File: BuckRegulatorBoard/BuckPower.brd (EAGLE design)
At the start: 41.6 x 31.7 mm, 5 parts, among them U1 LM2574N

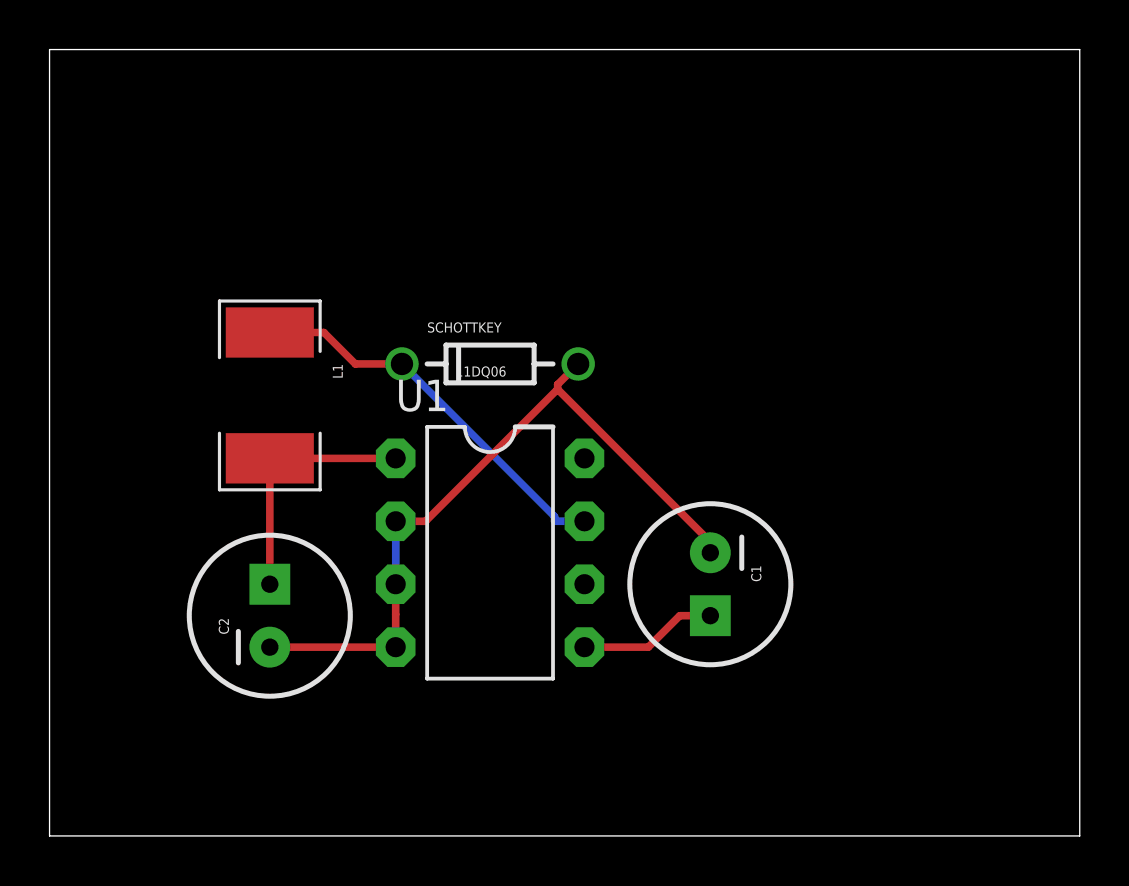
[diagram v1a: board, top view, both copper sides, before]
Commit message: Tested versions of breakout boards
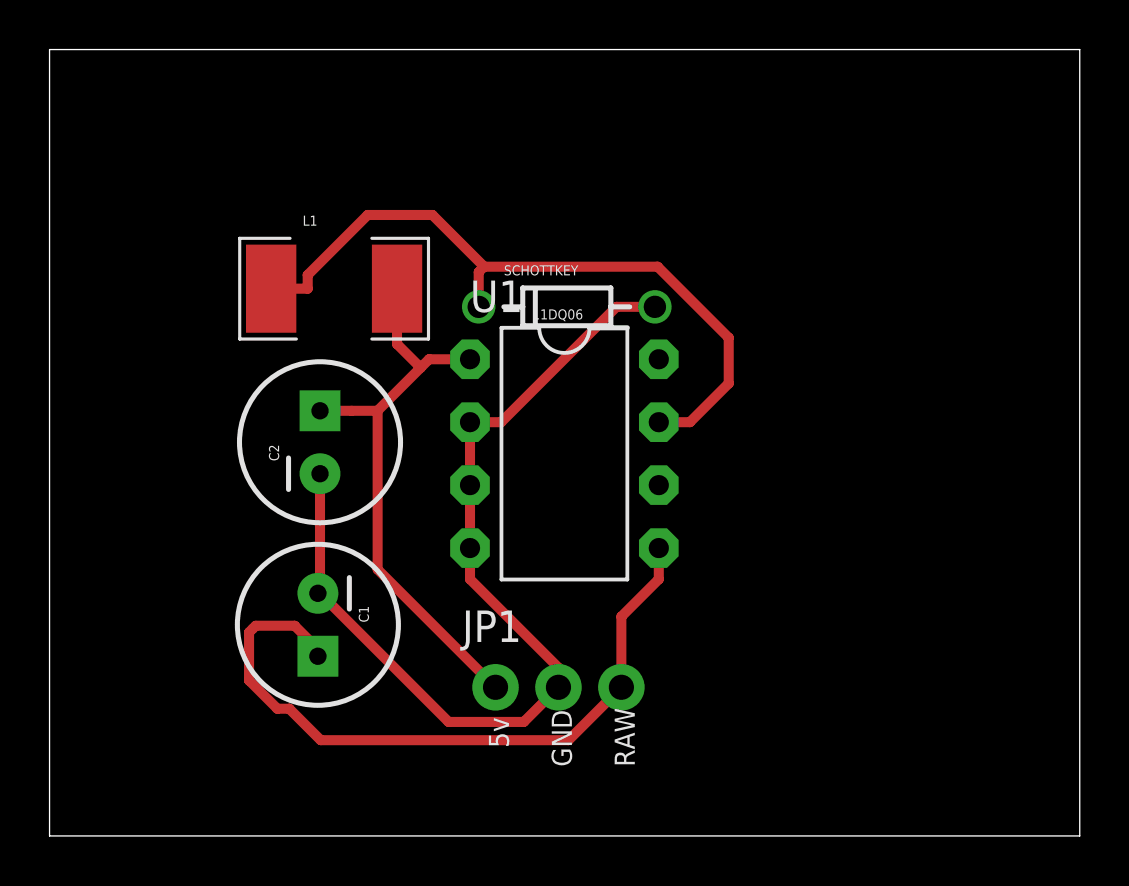
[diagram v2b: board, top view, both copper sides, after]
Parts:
- added JP1: (no value), SparkFun:1X03_NO_SILK
- moved C1 15.9 mm to (10.8, 8.52)
- moved C2 7.29 mm to (10.9, 15.9)
- moved L1 5.03 mm to (11.5, 22.1), turned to 0 degrees
- moved U1 5.00 mm to (20.8, 15.4)
- moved SCHOTTKEY 3.86 mm to (20.9, 21.4)
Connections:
- net GND: now also JP1.2
- net RAW: now also JP1.3
- net VCC: now also JP1.1
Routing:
- net RAW: track 5.61 -> 28.7 mm
- net VCC: track 10.2 -> 23.6 mm
- net N$1: track 16.0 -> 29.1 mm
- net GND: track 29.4 -> 38.8 mm
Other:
- board text added: "5v"
- board text added: "GND"
- board text added: "RAW"
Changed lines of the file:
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@@
 <setting verticaltext="up"/>
 </settings>
-<grid distance="1" unitdist="mm" unit="mm" style="lines" multiple="1" display="yes" altdistance="0.025" altunitdist="inch" altunit="inch"/>
+<grid distance="10" unitdist="mil" unit="mil" style="lines" multiple="1" display="yes" altdistance="1" altunitdist="mil" altunit="mil"/>
 <layers>
 <layer number="1" name="Top" color="4" fill="1" visible="yes" active="yes"/>
@@
 <wire x1="41.58" y1="31.74" x2="0" y2="31.74" width="0" layer="20"/>
 <wire x1="0" y1="31.74" x2="0" y2="0" width="0" layer="20"/>
+<rectangle x1="13.1064" y1="24.3078" x2="15.2654" y2="24.5618" layer="41"/>
+<rectangle x1="25.7048" y1="18.5166" x2="26.8986" y2="19.8628" layer="41"/>
+<text x="18.542" y="3.556" size="0.8128" layer="25" ratio="10" rot="R90">5v</text>
+<text x="21.082" y="2.794" size="0.8128" layer="25" ratio="10" rot="R90">GND</text>
+<text x="23.622" y="2.794" size="0.8128" layer="25" ratio="10" rot="R90">RAW</text>
 </plain>
 <attributes>
@@
 </autorouter>
 <elements>
-<element name="U1" library="Dustin" package="8DILL" value="LM2574N" x="17.78" y="11.43" rot="R270"/>
-<element name="C1" library="SparkFun" package="CPOL-RADIAL-100UF-25V" value="22uf" x="26.67" y="10.16" rot="R270"/>
-<element name="C2" library="SparkFun" package="CPOL-RADIAL-100UF-25V" value="220uf" x="8.89" y="8.89" rot="R90"/>
-<element name="L1" library="SparkFun" package="INDUCTOR-1206" value="330uH" x="8.89" y="17.78" rot="R270"/>
-<element name="SCHOTTKEY" library="SparkFun" package="DIODE-ZENER" value="11DQ06" x="17.78" y="19.05"/>
+<element name="U1" library="Dustin" package="8DILL" value="LM2574N" x="20.78" y="15.43" rot="R270"/>
+<element name="C1" library="SparkFun" package="CPOL-RADIAL-100UF-25V" value="22uf" x="10.8311" y="8.5228" rot="R270"/>
+<element name="C2" library="SparkFun" package="CPOL-RADIAL-100UF-25V" value="220uf" x="10.9165" y="15.89" rot="R90"/>
+<element name="L1" library="SparkFun" package="INDUCTOR-1206" value="330uH" x="11.485" y="22.089"/>
+<element name="SCHOTTKEY" library="SparkFun" package="DIODE-ZENER" value="11DQ06" x="20.8769" y="21.3553"/>
+<element name="JP1" library="SparkFun" package="1X03_NO_SILK" value="" x="18" y="6"/>
 </elements>
 <signals>
@@
 <contactref element="U1" pad="5"/>
 <contactref element="C1" pad="1"/>
-<wire x1="26.67" y1="8.89" x2="25.438" y2="8.89" width="0.3048" layer="1"/>
-<wire x1="21.59" y1="7.62" x2="24.168" y2="7.62" width="0.3048" layer="1"/>
-<wire x1="24.168" y1="7.62" x2="25.438" y2="8.89" width="0.3048" layer="1"/>
+<contactref element="JP1" pad="3"/>
+<wire x1="8.2024" y1="8.3661" x2="8.0517" y2="8.2154" width="0.4064" layer="1"/>
+<wire x1="8.0517" y1="8.2154" x2="8.0517" y2="6.277" width="0.4064" layer="1"/>
+<wire x1="8.0517" y1="6.277" x2="9.1946" y2="5.1341" width="0.4064" layer="1"/>
+<wire x1="9.1946" y1="5.1341" x2="9.6773" y2="5.1341" width="0.4064" layer="1"/>
+<wire x1="9.6773" y1="5.1341" x2="9.6773" y2="5.134" width="0.4064" layer="1"/>
+<wire x1="9.6773" y1="5.134" x2="10.9461" y2="3.8652" width="0.4064" layer="1"/>
+<wire x1="10.9461" y1="3.8652" x2="20.9452" y2="3.8652" width="0.4064" layer="1"/>
+<wire x1="20.9452" y1="3.8652" x2="23.08" y2="6" width="0.4064" layer="1"/>
+<wire x1="10.8311" y1="7.2528" x2="10.8311" y2="7.5486" width="0.4064" layer="1"/>
+<wire x1="10.8311" y1="7.5486" x2="9.896" y2="8.4837" width="0.4064" layer="1"/>
+<wire x1="9.896" y1="8.4837" x2="8.32" y2="8.4837" width="0.4064" layer="1"/>
+<wire x1="8.32" y1="8.4837" x2="8.2024" y2="8.3661" width="0.4064" layer="1"/>
+<wire x1="24.59" y1="10.3626" x2="23.08" y2="8.8526" width="0.4064" layer="1"/>
+<wire x1="23.08" y1="8.8526" x2="23.08" y2="6" width="0.4064" layer="1"/>
+<wire x1="24.59" y1="11.62" x2="24.59" y2="10.3626" width="0.4064" layer="1"/>
 </signal>
 <signal name="GND">
@@
 <contactref element="U1" pad="3"/>
 <contactref element="SCHOTTKEY" pad="P$2"/>
-<wire x1="20.5065" y1="18.0299" x2="26.67" y2="11.8663" width="0.3048" layer="1"/>
-<wire x1="26.67" y1="11.8663" x2="26.67" y2="11.43" width="0.3048" layer="1"/>
-<wire x1="21.336" y1="19.05" x2="20.5064" y2="18.2204" width="0.3048" layer="1"/>
-<wire x1="20.5064" y1="18.2204" x2="20.5064" y2="18.0299" width="0.3048" layer="1"/>
-<wire x1="20.5064" y1="18.0299" x2="20.5065" y2="18.0299" width="0.3048" layer="1"/>
-<wire x1="15.1766" y1="12.7" x2="20.5065" y2="18.0299" width="0.3048" layer="1"/>
-<wire x1="13.97" y1="12.7" x2="15.1766" y2="12.7" width="0.3048" layer="1"/>
-<wire x1="13.97" y1="7.62" x2="13.97" y2="8.9534" width="0.3048" layer="1"/>
-<wire x1="13.97" y1="7.62" x2="8.89" y2="7.62" width="0.3048" layer="1"/>
-<wire x1="13.97" y1="10.16" x2="13.97" y2="8.9534" width="0.3048" layer="1"/>
-<wire x1="13.97" y1="10.16" x2="13.97" y2="12.7" width="0.3048" layer="16"/>
+<contactref element="JP1" pad="2"/>
+<wire x1="10.9165" y1="9.7928" x2="16.1075" y2="4.6018" width="0.4064" layer="1"/>
+<wire x1="16.1075" y1="4.6018" x2="19.1418" y2="4.6018" width="0.4064" layer="1"/>
+<wire x1="19.1418" y1="4.6018" x2="20.54" y2="6" width="0.4064" layer="1"/>
+<wire x1="18.2274" y1="16.7" x2="22.8827" y2="21.3553" width="0.4064" layer="1"/>
+<wire x1="22.8827" y1="21.3553" x2="24.4329" y2="21.3553" width="0.4064" layer="1"/>
+<wire x1="10.9165" y1="9.7928" x2="10.8311" y2="9.7928" width="0.4064" layer="1"/>
+<wire x1="10.9165" y1="14.62" x2="10.9165" y2="9.7928" width="0.4064" layer="1"/>
+<wire x1="16.97" y1="10.3626" x2="20.54" y2="6.7926" width="0.4064" layer="1"/>
+<wire x1="20.54" y1="6.7926" x2="20.54" y2="6" width="0.4064" layer="1"/>
+<wire x1="16.97" y1="11.62" x2="16.97" y2="10.3626" width="0.4064" layer="1"/>
+<wire x1="16.97" y1="14.16" x2="16.97" y2="11.62" width="0.4064" layer="1"/>
+<wire x1="16.97" y1="16.7" x2="18.2274" y2="16.7" width="0.4064" layer="1"/>
+<wire x1="16.97" y1="14.16" x2="16.97" y2="16.7" width="0.4064" layer="1"/>
 </signal>
 <signal name="N$1">
@@
 <contactref element="U1" pad="7"/>
 <contactref element="SCHOTTKEY" pad="P$1"/>
-<wire x1="21.59" y1="12.7" x2="20.3834" y2="12.7" width="0.3048" layer="16"/>
-<wire x1="20.3834" y1="12.7" x2="20.3834" y2="12.8906" width="0.3048" layer="16"/>
-<wire x1="20.3834" y1="12.8906" x2="14.224" y2="19.05" width="0.3048" layer="16"/>
-<wire x1="8.89" y1="20.32" x2="11.0745" y2="20.32" width="0.3048" layer="1"/>
-<wire x1="14.224" y1="19.05" x2="12.3445" y2="19.05" width="0.3048" layer="1"/>
-<wire x1="12.3445" y1="19.05" x2="11.0745" y2="20.32" width="0.3048" layer="1"/>
+<wire x1="17.5409" y1="22.9765" x2="17.3209" y2="22.7565" width="0.4064" layer="1"/>
+<wire x1="17.3209" y1="22.7565" x2="17.3209" y2="21.3553" width="0.4064" layer="1"/>
+<wire x1="17.5409" y1="22.9765" x2="24.5432" y2="22.9765" width="0.4064" layer="1"/>
+<wire x1="24.5432" y1="22.9765" x2="27.4124" y2="20.1073" width="0.4064" layer="1"/>
+<wire x1="27.4124" y1="20.1073" x2="27.4124" y2="18.265" width="0.4064" layer="1"/>
+<wire x1="27.4124" y1="18.265" x2="25.8474" y2="16.7" width="0.4064" layer="1"/>
+<wire x1="24.59" y1="16.7" x2="25.8474" y2="16.7" width="0.4064" layer="1"/>
+<wire x1="17.5409" y1="22.9765" x2="15.4548" y2="25.0626" width="0.4064" layer="1"/>
+<wire x1="15.4548" y1="25.0626" x2="12.8394" y2="25.0626" width="0.4064" layer="1"/>
+<wire x1="12.8394" y1="25.0626" x2="10.4183" y2="22.6415" width="0.4064" layer="1"/>
+<wire x1="10.4183" y1="22.6415" x2="10.4183" y2="22.089" width="0.4064" layer="1"/>
+<wire x1="8.945" y1="22.089" x2="10.4183" y2="22.089" width="0.4064" layer="1"/>
 </signal>
 <signal name="VCC">
@@
 <contactref element="L1" pad="P$2"/>
 <contactref element="U1" pad="1"/>
-<wire x1="8.89" y1="15.24" x2="8.89" y2="10.16" width="0.3048" layer="1"/>
-<wire x1="13.97" y1="15.24" x2="8.89" y2="15.24" width="0.3048" layer="1"/>
+<contactref element="JP1" pad="1"/>
+<wire x1="14.979" y1="18.8997" x2="13.2393" y2="17.16" width="0.4064" layer="1"/>
+<wire x1="16.97" y1="19.24" x2="15.3193" y2="19.24" width="0.4064" layer="1"/>
+<wire x1="15.3193" y1="19.24" x2="14.979" y2="18.8997" width="0.4064" layer="1"/>
+<wire x1="14.025" y1="19.8537" x2="14.979" y2="18.8997" width="0.4064" layer="1"/>
+<wire x1="14.025" y1="22.089" x2="14.025" y2="19.8537" width="0.4064" layer="1"/>
+<wire x1="13.2393" y1="17.16" x2="13.2393" y2="10.7607" width="0.4064" layer="1"/>
+<wire x1="13.2393" y1="10.7607" x2="18" y2="6" width="0.4064" layer="1"/>
+<wire x1="12.1993" y1="17.16" x2="13.2393" y2="17.16" width="0.4064" layer="1"/>
+<wire x1="10.9165" y1="17.16" x2="12.1993" y2="17.16" width="0.4064" layer="1"/>
 </signal>
 </signals>
